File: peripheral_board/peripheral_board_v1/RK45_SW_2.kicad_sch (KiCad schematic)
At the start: 10 parts

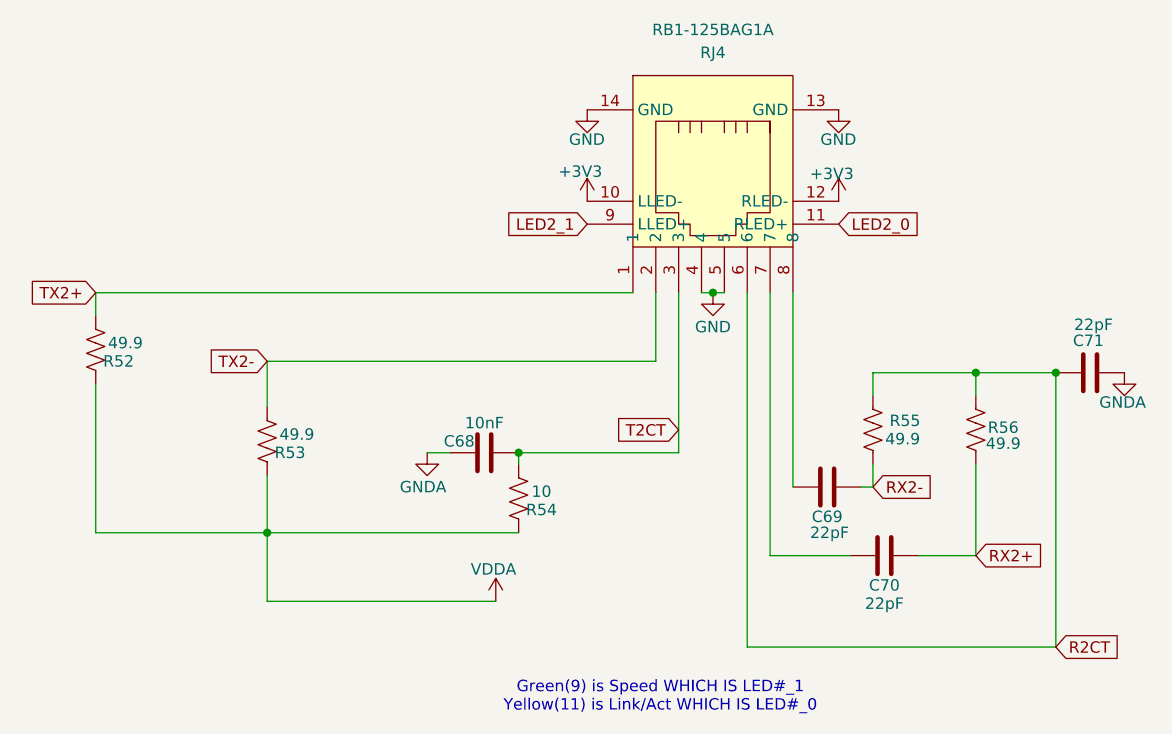
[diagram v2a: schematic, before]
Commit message: Schematic design ready for review
Made the last changes for the Wiznet by adding in Dip switches and made sure that the interrupt and reset signals are attached to the raspberry pi.

Finished the Etherent switch by wiring the RJ45 port 1 with 2 configurations, leaning more towards not using the Wiznet port but might do it any ways for cost. Added test points to port 5 but might change it to be RMII configuration because the 4 port strap in mode sets it to that config. Put solder jumpers in for the LED strap in mode. On the schematic I put in a note about how to configure to the proper mode we want but after a review will change to be a hardwire set. Made the reset switch match that of the EVAL board but further reading found I do not need the diode. Created the VDDIO and VDDAT which are just 2 different versions of 3.3V. Layout would be next but need to learn more about trace integrity and impedance control.
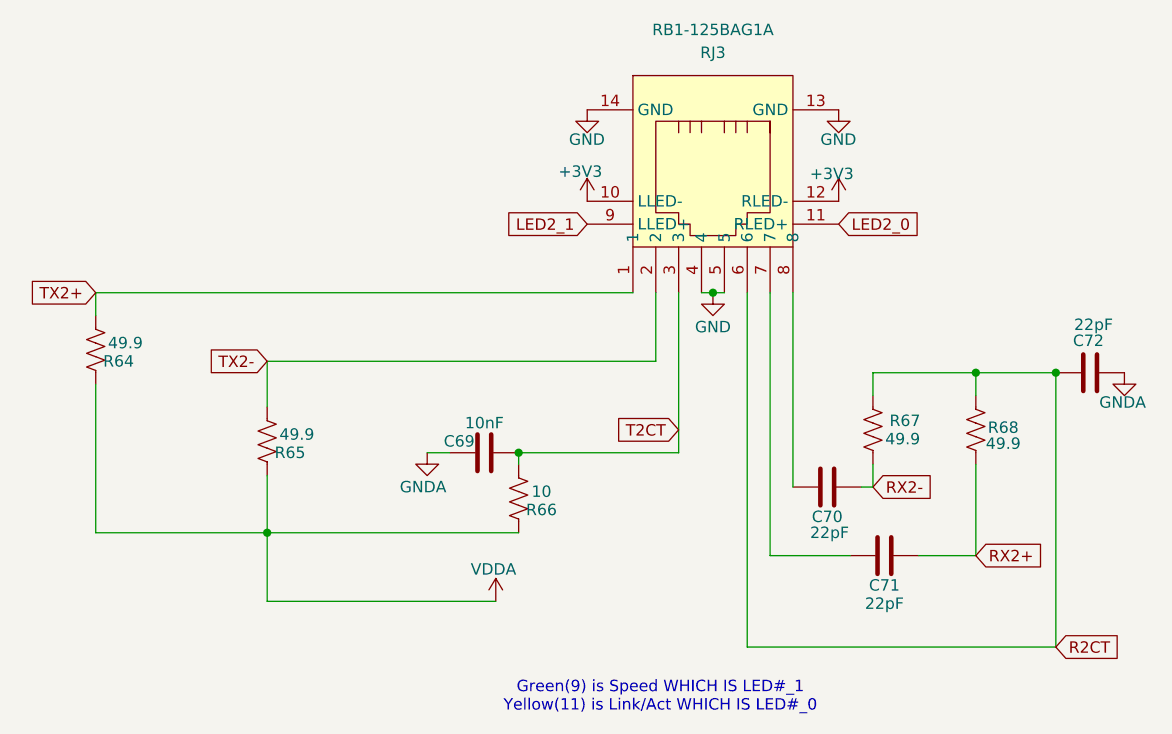
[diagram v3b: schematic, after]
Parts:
- renumbered C68 to C69, C69 to C70, C70 to C71, C71 to C72, R52 to R64, R53 to R65, R54 to R66, R55 to R67, R56 to R68, RJ4 to RJ3
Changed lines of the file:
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@@
 		(on_board yes)
 		(dnp no)
-		(property "Reference" "#PWR0133"
+		(property "Reference" "#PWR0156"
 			(at 250.19 110.49 0)
 			(effects
@@
 			(project "peripheral_board"
 				(path "/14f8712f-1710-40cb-b01e-cc9b3c4405bd/bdffb641-9271-40a7-b849-e20d9ae38619/e33b6a68-dc96-48cc-8464-e4dc3509a86a"
-					(reference "#PWR0133")
+					(reference "#PWR0156")
 					(unit 1)
 				)
@@
 		(on_board yes)
 		(dnp no)
-		(property "Reference" "#PWR0131"
+		(property "Reference" "#PWR0154"
 			(at 236.22 123.19 0)
 			(effects
@@
 			(project "peripheral_board"
 				(path "/14f8712f-1710-40cb-b01e-cc9b3c4405bd/bdffb641-9271-40a7-b849-e20d9ae38619/e33b6a68-dc96-48cc-8464-e4dc3509a86a"
-					(reference "#PWR0131")
+					(reference "#PWR0154")
 					(unit 1)
 				)
@@
 		(on_board yes)
 		(dnp no)
-		(property "Reference" "R53"
+		(property "Reference" "R65"
 			(at 189.23 134.62 0)
 			(effects
@@
 			(project "peripheral_board"
 				(path "/14f8712f-1710-40cb-b01e-cc9b3c4405bd/bdffb641-9271-40a7-b849-e20d9ae38619/e33b6a68-dc96-48cc-8464-e4dc3509a86a"
-					(reference "R53")
+					(reference "R65")
 					(unit 1)
 				)
@@
 		(on_board yes)
 		(dnp no)
-		(property "Reference" "R56"
+		(property "Reference" "R68"
 			(at 268.478 131.826 0)
 			(effects
@@
 			(project "peripheral_board"
 				(path "/14f8712f-1710-40cb-b01e-cc9b3c4405bd/bdffb641-9271-40a7-b849-e20d9ae38619/e33b6a68-dc96-48cc-8464-e4dc3509a86a"
-					(reference "R56")
+					(reference "R68")
 					(unit 1)
 				)
@@
 		(dnp no)
 		(fields_autoplaced yes)
-		(property "Reference" "RJ4"
+		(property "Reference" "RJ3"
 			(at 236.22 90.17 0)
 			(effects
@@
 			(project "peripheral_board"
 				(path "/14f8712f-1710-40cb-b01e-cc9b3c4405bd/bdffb641-9271-40a7-b849-e20d9ae38619/e33b6a68-dc96-48cc-8464-e4dc3509a86a"
-					(reference "RJ4")
+					(reference "RJ3")
 					(unit 1)
 				)
@@
 		(on_board yes)
 		(dnp no)
-		(property "Reference" "#PWR0130"
+		(property "Reference" "#PWR0153"
 			(at 222.25 110.49 0)
 			(effects
@@
 			(project "peripheral_board"
 				(path "/14f8712f-1710-40cb-b01e-cc9b3c4405bd/bdffb641-9271-40a7-b849-e20d9ae38619/e33b6a68-dc96-48cc-8464-e4dc3509a86a"
-					(reference "#PWR0130")
+					(reference "#PWR0153")
 					(unit 1)
 				)
@@
 		(on_board yes)
 		(dnp no)
-		(property "Reference" "C69"
+		(property "Reference" "C70"
 			(at 248.92 141.732 90)
 			(effects
@@
 			(project "peripheral_board"
 				(path "/14f8712f-1710-40cb-b01e-cc9b3c4405bd/bdffb641-9271-40a7-b849-e20d9ae38619/e33b6a68-dc96-48cc-8464-e4dc3509a86a"
-					(reference "C69")
+					(reference "C70")
 					(unit 1)
 				)
@@
 		(on_board yes)
 		(dnp no)
-		(property "Reference" "#PWR0127"
+		(property "Reference" "#PWR0150"
 			(at 204.47 140.97 0)
 			(effects
@@
 			(project "peripheral_board"
 				(path "/14f8712f-1710-40cb-b01e-cc9b3c4405bd/bdffb641-9271-40a7-b849-e20d9ae38619/e33b6a68-dc96-48cc-8464-e4dc3509a86a"
-					(reference "#PWR0127")
+					(reference "#PWR0150")
 					(unit 1)
 				)
@@
 		(on_board yes)
 		(dnp no)
-		(property "Reference" "R55"
+		(property "Reference" "R67"
 			(at 257.556 131.064 0)
 			(effects
@@
 			(project "peripheral_board"
 				(path "/14f8712f-1710-40cb-b01e-cc9b3c4405bd/bdffb641-9271-40a7-b849-e20d9ae38619/e33b6a68-dc96-48cc-8464-e4dc3509a86a"
-					(reference "R55")
+					(reference "R67")
 					(unit 1)
 				)
@@
 		(on_board yes)
 		(dnp no)
-		(property "Reference" "C68"
+		(property "Reference" "C69"
 			(at 208.026 133.35 90)
 			(effects
@@
 			(project "peripheral_board"
 				(path "/14f8712f-1710-40cb-b01e-cc9b3c4405bd/bdffb641-9271-40a7-b849-e20d9ae38619/e33b6a68-dc96-48cc-8464-e4dc3509a86a"
-					(reference "C68")
+					(reference "C69")
 					(unit 1)
 				)
@@
 		(on_board yes)
 		(dnp no)
-		(property "Reference" "#PWR0129"
+		(property "Reference" "#PWR0152"
 			(at 222.25 102.87 0)
 			(effects
@@
 			(project "peripheral_board"
 				(path "/14f8712f-1710-40cb-b01e-cc9b3c4405bd/bdffb641-9271-40a7-b849-e20d9ae38619/e33b6a68-dc96-48cc-8464-e4dc3509a86a"
-					(reference "#PWR0129")
+					(reference "#PWR0152")
 					(unit 1)
 				)
@@
 		(on_board yes)
 		(dnp no)
-		(property "Reference" "R54"
+		(property "Reference" "R66"
 			(at 217.17 140.97 0)
 			(effects
@@
 			(project "peripheral_board"
 				(path "/14f8712f-1710-40cb-b01e-cc9b3c4405bd/bdffb641-9271-40a7-b849-e20d9ae38619/e33b6a68-dc96-48cc-8464-e4dc3509a86a"
-					(reference "R54")
+					(reference "R66")
 					(unit 1)
 				)
@@
 		(on_board yes)
 		(dnp no)
-		(property "Reference" "#PWR0132"
+		(property "Reference" "#PWR0155"
 			(at 250.19 102.87 0)
 			(effects
@@
 			(project "peripheral_board"
 				(path "/14f8712f-1710-40cb-b01e-cc9b3c4405bd/bdffb641-9271-40a7-b849-e20d9ae38619/e33b6a68-dc96-48cc-8464-e4dc3509a86a"
-					(reference "#PWR0132")
+					(reference "#PWR0155")
 					(unit 1)
 				)
@@
 		(on_board yes)
 		(dnp no)
-		(property "Reference" "#PWR0134"
+		(property "Reference" "#PWR0157"
 			(at 281.94 132.08 0)
 			(effects
@@
 			(project "peripheral_board"
 				(path "/14f8712f-1710-40cb-b01e-cc9b3c4405bd/bdffb641-9271-40a7-b849-e20d9ae38619/e33b6a68-dc96-48cc-8464-e4dc3509a86a"
-					(reference "#PWR0134")
+					(reference "#PWR0157")
 					(unit 1)
 				)
@@
 		(on_board yes)
 		(dnp no)
-		(property "Reference" "C70"
+		(property "Reference" "C71"
 			(at 255.27 149.352 90)
 			(effects
@@
 			(project "peripheral_board"
 				(path "/14f8712f-1710-40cb-b01e-cc9b3c4405bd/bdffb641-9271-40a7-b849-e20d9ae38619/e33b6a68-dc96-48cc-8464-e4dc3509a86a"
-					(reference "C70")
+					(reference "C71")
 					(unit 1)
 				)
@@
 		(on_board yes)
 		(dnp no)
-		(property "Reference" "C71"
+		(property "Reference" "C72"
 			(at 279.654 122.174 90)
 			(effects
@@
 			(project "peripheral_board"
 				(path "/14f8712f-1710-40cb-b01e-cc9b3c4405bd/bdffb641-9271-40a7-b849-e20d9ae38619/e33b6a68-dc96-48cc-8464-e4dc3509a86a"
-					(reference "C71")
+					(reference "C72")
 					(unit 1)
 				)
@@
 		(on_board yes)
 		(dnp no)
-		(property "Reference" "R52"
+		(property "Reference" "R64"
 			(at 170.18 124.46 0)
 			(effects
@@
 			(project "peripheral_board"
 				(path "/14f8712f-1710-40cb-b01e-cc9b3c4405bd/bdffb641-9271-40a7-b849-e20d9ae38619/e33b6a68-dc96-48cc-8464-e4dc3509a86a"
-					(reference "R52")
+					(reference "R64")
 					(unit 1)
 				)
@@
 		(on_board yes)
 		(dnp no)
-		(property "Reference" "#PWR0128"
+		(property "Reference" "#PWR0151"
 			(at 212.09 154.94 0)
 			(effects
@@
 			(project "peripheral_board"
 				(path "/14f8712f-1710-40cb-b01e-cc9b3c4405bd/bdffb641-9271-40a7-b849-e20d9ae38619/e33b6a68-dc96-48cc-8464-e4dc3509a86a"
-					(reference "#PWR0128")
-					(unit 1)
-				)
+					(reference "#PWR0151")
+					(unit 1)
+				)

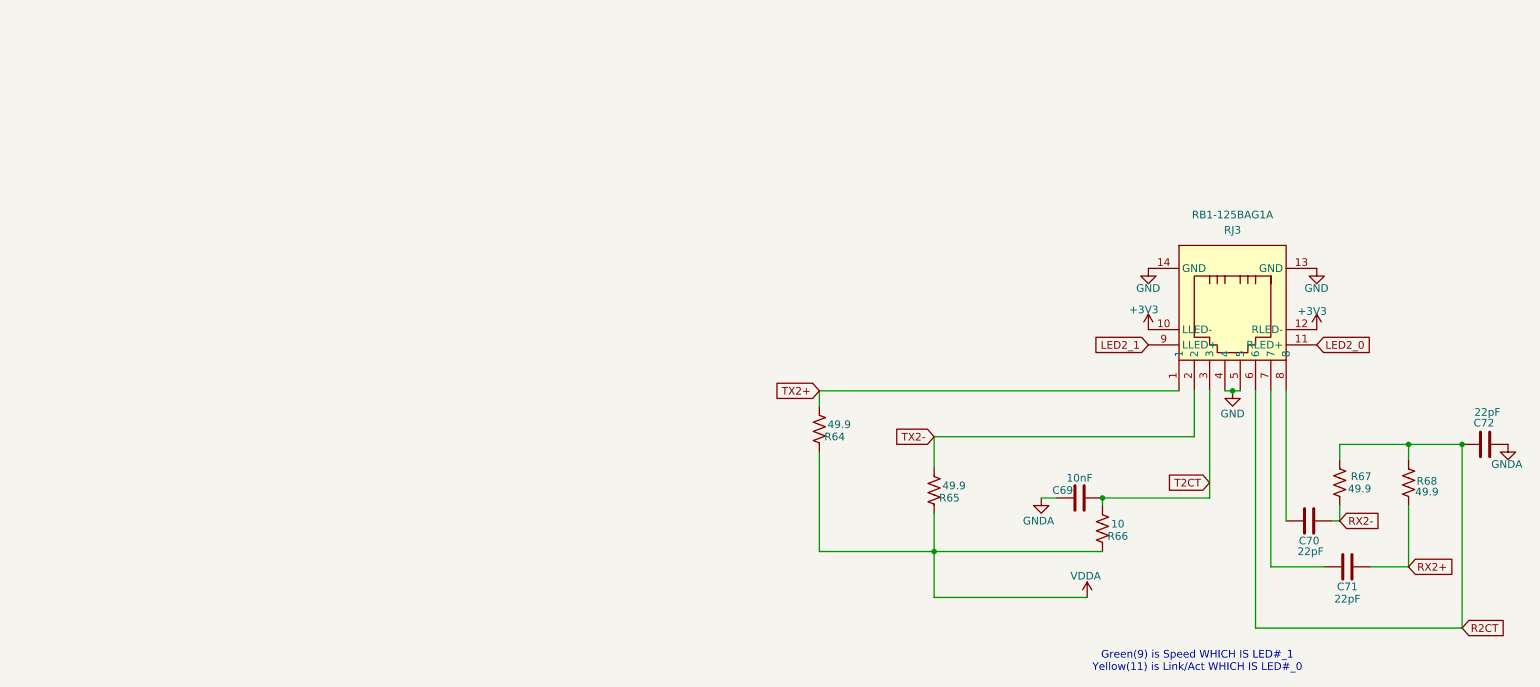
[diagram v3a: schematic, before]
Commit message: Started the PCB layout
Finished the schematic. Now working on the PCB. Might looking in to moving to a 6 layer board.
Need to do a bit of redesign because changing some of the parts had different footprints.

Started on the Wiznet and the its RJ45 port it has. Want to make the port close to the chip as a possible. Currently working on the 4 layer stack up but if I switch to a 6 layer it might help with impedance and change the overall signal layering.
Almost done with the Wiznet just need to do the clock and the TX/RX pairs.
Once that is done I will work on the Ethernet switch then lastly the breakout pins for the RP.

I should have selected either a 6 layer or 4 layer board, leaning more towards 6 layer because I can keep my signals separated by the 3 and 3 sections.
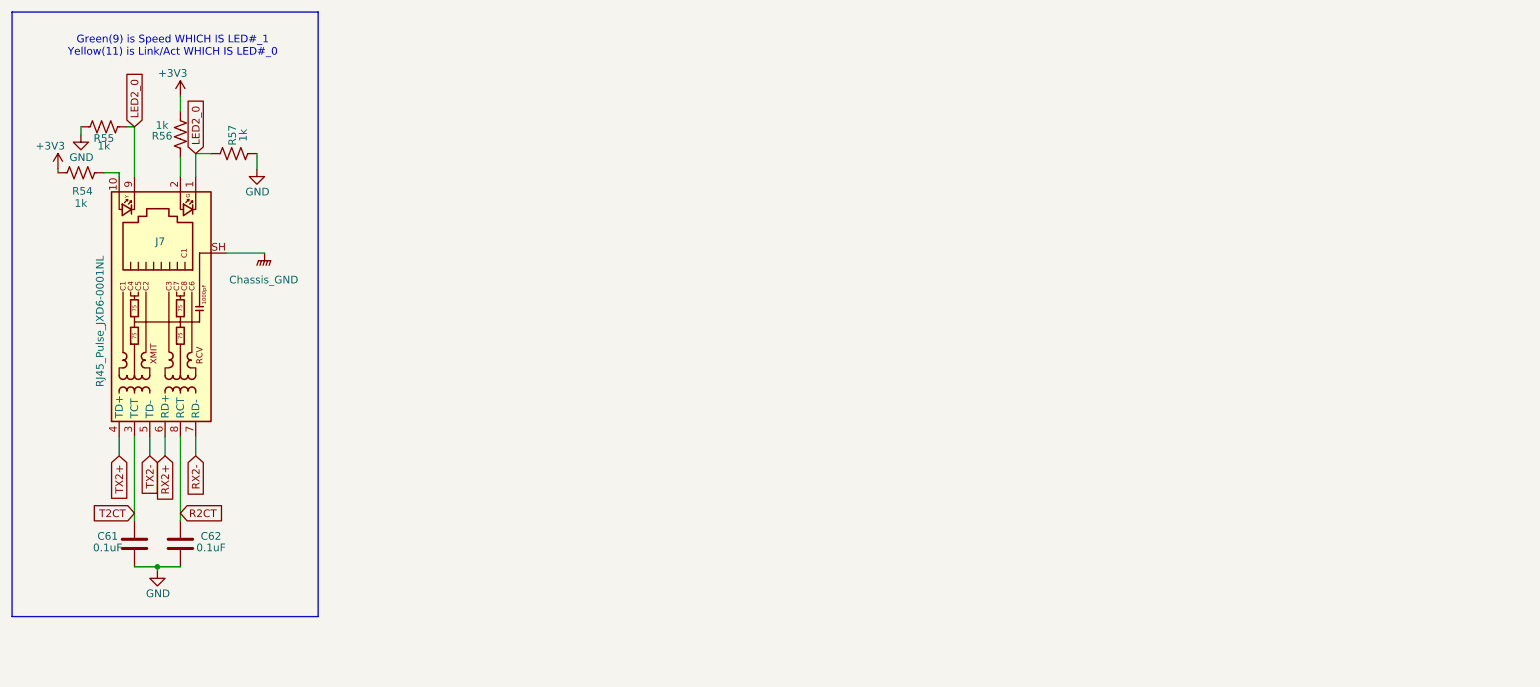
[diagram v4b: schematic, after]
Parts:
- removed C69: 10nF, Capacitor_SMD:C_0402_1005Metric, symbol Device:C
- removed C70, C71, C72: 22pF, Capacitor_SMD:C_0402_1005Metric, symbol Device:C
- removed R64, R65, R67, R68: 49.9, Resistor_SMD:R_0603_1608Metric, symbol Device:R_US
- removed R66: 10, Resistor_SMD:R_0603_1608Metric, symbol Device:R_US
- removed RJ3: RB1-125BAG1A, easyeda2kicad:RJ45-TH_RB1-125BAG1A, symbol easyeda2kicad:RB1-125BAG1A
- added C61, C62: 0.1uF, Capacitor_SMD:C_0402_1005Metric, symbol Device:C
- added J7: RJ45_Pulse_JXD6-0001NL, Connector_RJ:RJ45_Pulse_JXD6-0001NL_Horizontal, symbol Connector:RJ45_Pulse_JXD6-0001NL
- added R54, R55, R56, R57: 1k, Resistor_SMD:R_0603_1608Metric, symbol Device:R_US
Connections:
- net +3V3: now also R54.2, R56.2
- net GND: now also C61.2, C62.2, R55.2, R57.2
- net LED2_0: now also J7.1, J7.9, R55.1, R57.1
- net R2CT: now also C62.1, J7.8 (RCT)
- net RX2+: now also J7.6 (RD+)
- net RX2-: now also J7.7 (RD-)
- net T2CT: now also C61.1, J7.3 (TCT)
- net TX2+: now also J7.4 (TD+)
- net TX2-: now also J7.5 (TD-)
- new net: J7.10, R54.1
- new net: J7.2, R56.1
- new net Chassis_GND: J7.SH
